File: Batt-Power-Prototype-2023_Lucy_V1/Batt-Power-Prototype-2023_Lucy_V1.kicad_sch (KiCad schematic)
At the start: 49 parts, among them J3 DE9_Receptacle_MountingHoles

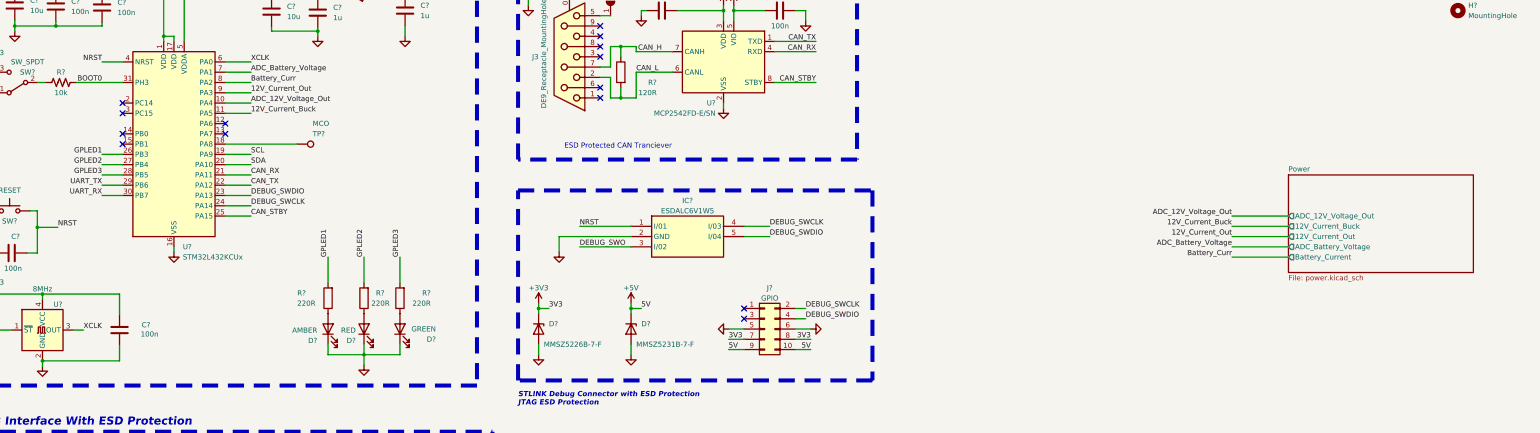
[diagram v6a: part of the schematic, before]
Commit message: everything but the battery input done
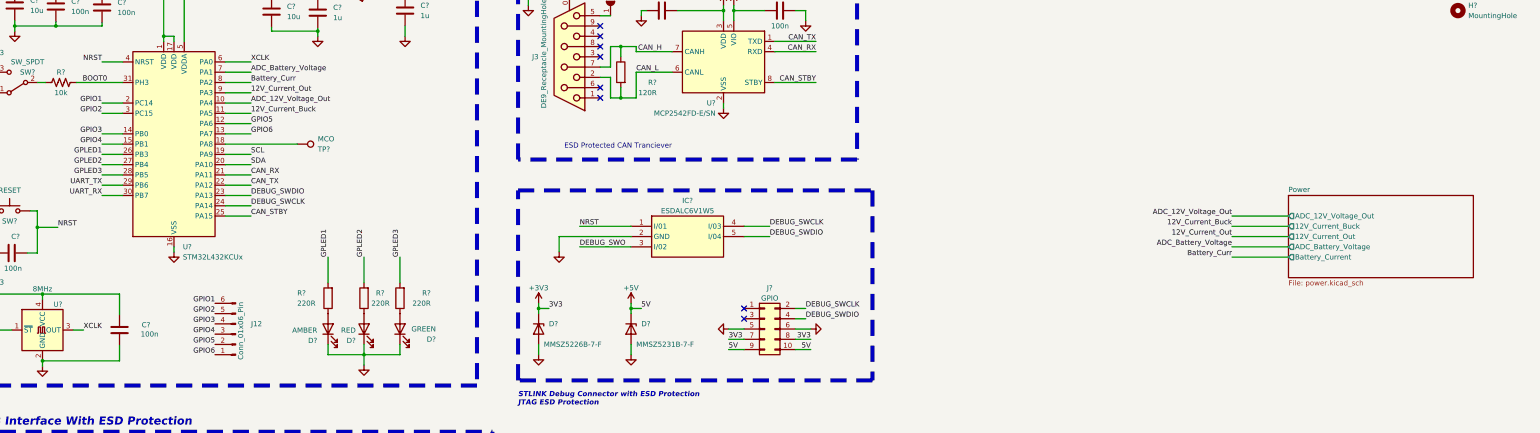
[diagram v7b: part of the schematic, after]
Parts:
- added J12: Conn_01x06_Pin, Connector_TE-Connectivity:TE_826576-6_1x06_P3.96mm_Vertical, symbol Connector:Conn_01x06_Pin
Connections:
- net GPIO5: now reaches U?.12 (PA6)
- net GPIO5: now also J12.2 (Pin_2)
- net GPIO6: now reaches U?.13 (PA7)
- net GPIO6: now also J12.1 (Pin_1)
- net GPIO3: now reaches U?.14 (PB0)
- net GPIO3: now also J12.4 (Pin_4)
- net GPIO4: now reaches U?.15 (PB1)
- net GPIO4: now also J12.3 (Pin_3)
- net GPIO1: now reaches U?.2 (PC14)
- net GPIO1: now also J12.6 (Pin_6)
- net GPIO2: now reaches U?.3 (PC15)
- net GPIO2: now also J12.5 (Pin_5)
- no-connect marks 19 -> 13
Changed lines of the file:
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@@
   (no_connect (at 176.53 45.72))
   (no_connect (at 54.61 160.02))
-  (no_connect (at 58.42 57.15))
   (no_connect (at 212.09 110.49))
-  (no_connect (at 58.42 59.69))
   (no_connect (at 176.53 53.34))
   (no_connect (at 31.75 167.64))
-  (no_connect (at 83.82 64.77))
   (no_connect (at 176.53 43.18))
   (no_connect (at 212.09 107.95))
   (no_connect (at 176.53 40.64))
-  (no_connect (at 58.42 67.31))
-  (no_connect (at 58.42 64.77))
   (no_connect (at 176.53 38.1))
   (no_connect (at 54.61 165.1))
-  (no_connect (at 83.82 62.23))
   (no_connect (at 31.75 162.56))
   (no_connect (at 176.53 55.88))
@@
     (stroke (width 0) (type default))
   )
+  (wire (pts (xy 83.82 62.23) (xy 90.17 62.23))
+    (stroke (width 0) (type default))
+  )
   (wire (pts (xy 57.15 147.32) (xy 55.88 147.32))
     (stroke (width 0) (type default))
@@
     (stroke (width 0) (type default))
   )
+  (wire (pts (xy 53.34 64.77) (xy 58.42 64.77))
+    (stroke (width 0) (type default))
+  )
   (wire (pts (xy 49.53 190.5) (xy 49.53 191.77))
     (stroke (width 0) (type default))
@@
     (stroke (width 0) (type default))
   )
+  (wire (pts (xy 53.34 59.69) (xy 58.42 59.69))
+    (stroke (width 0) (type default))
+  )
   (wire (pts (xy 186.69 34.29) (xy 186.69 35.56))
     (stroke (width 0) (type default))
@@
     (stroke (width 0) (type default))
   )
+  (wire (pts (xy 83.82 64.77) (xy 90.17 64.77))
+    (stroke (width 0) (type default))
+  )
   (wire (pts (xy 88.9 166.37) (xy 88.9 167.64))
     (stroke (width 0) (type default))
@@
     (stroke (width 0) (type default))
   )
+  (wire (pts (xy 53.34 67.31) (xy 58.42 67.31))
+    (stroke (width 0) (type default))
+  )
   (wire (pts (xy 31.75 38.1) (xy 31.75 39.37))
     (stroke (width 0) (type default))
@@
     (stroke (width 0) (type default))
   )
+  (wire (pts (xy 53.34 57.15) (xy 58.42 57.15))
+    (stroke (width 0) (type default))
+  )
   (wire (pts (xy 30.48 180.34) (xy 30.48 182.88))
     (stroke (width 0) (type default))
@@
     (effects (font (size 1.27 1.27)) (justify left bottom))
   )
+  (label "GPIO3" (at 81.28 111.76 180) (fields_autoplaced)
+    (effects (font (size 1.27 1.27)) (justify right bottom))
+  )
   (label "5V" (at 186.69 107.95 0) (fields_autoplaced)
     (effects (font (size 1.27 1.27)) (justify left bottom))
@@
     (effects (font (size 1.27 1.27)) (justify left bottom))
   )
+  (label "GPIO5" (at 81.28 116.84 180) (fields_autoplaced)
+    (effects (font (size 1.27 1.27)) (justify right bottom))
+  )
   (label "5V" (at 208.28 118.11 0) (fields_autoplaced)
     (effects (font (size 1.27 1.27)) (justify left bottom))
   )
+  (label "GPIO1" (at 81.28 106.68 180) (fields_autoplaced)
+    (effects (font (size 1.27 1.27)) (justify right bottom))
+  )
   (label "GPLED1" (at 53.34 69.85 180) (fields_autoplaced)
     (effects (font (size 1.27 1.27)) (justify right bottom))
@@
     (effects (font (size 1.27 1.27)) (justify right bottom))
   )
+  (label "GPIO2" (at 81.28 109.22 180) (fields_autoplaced)
+    (effects (font (size 1.27 1.27)) (justify right bottom))
+  )
+  (label "GPIO5" (at 90.17 62.23 0) (fields_autoplaced)
+    (effects (font (size 1.27 1.27)) (justify left bottom))
+  )
+  (label "GPIO6" (at 90.17 64.77 0) (fields_autoplaced)
+    (effects (font (size 1.27 1.27)) (justify left bottom))
+  )
   (label "DEBUG_SWDIO" (at 90.17 80.01 0) (fields_autoplaced)
     (effects (font (size 1.27 1.27)) (justify left bottom))
   )
+  (label "GPIO3" (at 53.34 64.77 180) (fields_autoplaced)
+    (effects (font (size 1.27 1.27)) (justify right bottom))
+  )
   (label "UART_RX" (at 53.34 80.01 180) (fields_autoplaced)
     (effects (font (size 1.27 1.27)) (justify right bottom))
@@
     (effects (font (size 1.27 1.27)) (justify right bottom))
   )
+  (label "GPIO1" (at 53.34 57.15 180) (fields_autoplaced)
+    (effects (font (size 1.27 1.27)) (justify right bottom))
+  )
+  (label "GPIO6" (at 81.28 119.38 180) (fields_autoplaced)
+    (effects (font (size 1.27 1.27)) (justify right bottom))
+  )
   (label "GPLED2" (at 118.11 95.25 90) (fields_autoplaced)
     (effects (font (size 1.27 1.27)) (justify left bottom))
@@
     (effects (font (size 1.27 1.27)) (justify left bottom))
   )
+  (label "GPIO2" (at 53.34 59.69 180) (fields_autoplaced)
+    (effects (font (size 1.27 1.27)) (justify right bottom))
+  )
   (label "CAN_STBY" (at 90.17 85.09 0) (fields_autoplaced)
     (effects (font (size 1.27 1.27)) (justify left bottom))
@@
     (effects (font (size 1.27 1.27)) (justify right bottom))
   )
-  (label "BOOT0" (at 53.34 52.07 180) (fields_autoplaced)
+  (label "BOOT0" (at 54.61 52.07 180) (fields_autoplaced)
     (effects (font (size 1.27 1.27)) (justify right bottom))
   )
@@
     (effects (font (size 1.27 1.27)) (justify right bottom))
   )
+  (label "GPIO4" (at 53.34 67.31 180) (fields_autoplaced)
+    (effects (font (size 1.27 1.27)) (justify right bottom))
+  )
+  (label "GPIO4" (at 81.28 114.3 180) (fields_autoplaced)
+    (effects (font (size 1.27 1.27)) (justify right bottom))
+  )
   (label "NRST" (at 53.34 46.99 180) (fields_autoplaced)
     (effects (font (size 1.27 1.27)) (justify right bottom))
@@
   (symbol (lib_id "Connector:TestPoint") (at 101.6 67.31 270) (unit 1)
     (in_bom yes) (on_board yes) (dnp no)
-    (property "Reference" "TP?" (at 105.41 64.77 90)
+    (property "Reference" "TP?" (at 106.68 68.58 90)
       (effects (font (size 1.27 1.27)) (justify left))
     )
-    (property "Value" "MCO" (at 105.41 62.23 90)
+    (property "Value" "MCO" (at 106.68 66.04 90)
       (effects (font (size 1.27 1.27)) (justify left))
     )
@@
     )
   )
+  (symbol (lib_id "Connector:Conn_01x06_Pin") (at 86.36 114.3 180) (unit 1)
+    (in_bom yes) (on_board yes) (dnp no)
+    (property "Reference" "J12" (at 90.17 111.76 0)
+      (effects (font (size 1.27 1.27)) (justify right))
+    )
+    (property "Value" "Conn_01x06_Pin" (at 87.63 120.65 90)
+      (effects (font (size 1.27 1.27)) (justify right))
+    )
+    (property "Footprint" "Connector_TE-Connectivity:TE_826576-6_1x06_P3.96mm_Vertical" (at 86.36 114.3 0)
+      (effects (font (size 1.27 1.27)) hide)
+    )
+    (property "Datasheet" "~" (at 86.36 114.3 0)
+      (effects (font (size 1.27 1.27)) hide)
+    )
+    (pin "1")
+    (pin "2")
+    (pin "3")
+    (pin "4")
+    (pin "5")
+    (pin "6")
+    (instances
+      (project "Batt-Power-Prototype-2023_Lucy_V1"
+        (path "/c58627b7-5b67-4b57-b29b-cc34a75a9096"
+          (reference "J12") (unit 1)
+        )
+      )
+    )
+  )
   (symbol (lib_id "MCU_ST_STM32L4:STM32L432KCUx") (at 71.12 67.31 0) (unit 1)
     (in_bom yes) (on_board yes) (dnp no) (fields_autoplaced)
@@
     )
   )
-  (sheet (at 346.71 74.93) (size 45.72 24.13) (fields_autoplaced)
+  (sheet (at 346.71 80.01) (size 45.72 20.32) (fields_autoplaced)
     (stroke (width 0.1524) (type solid))
     (fill (color 0 0 0 0.0000))
-    (property "Sheetname" "Power" (at 346.71 74.2184 0)
+    (property "Sheetname" "Power" (at 346.71 79.2984 0)
       (effects (font (size 1.27 1.27)) (justify left bottom))
     )
-    (property "Sheetfile" "power.kicad_sch" (at 346.71 99.6446 0)
+    (property "Sheetfile" "power.kicad_sch" (at 346.71 100.9146 0)
       (effects (font (size 1.27 1.27)) (justify left top))
     )

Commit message: everything done?!
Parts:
- C? (x2): JLCPCB Part#(optional) C1671 -> (none)
- C? (x9): JLCPCB Part#(optional) C1525 -> (none)
- C?: JLCPCB Part#(optional) C1779 -> (none)
- C? (x2): JLCPCB Part#(optional) C96446 -> (none)
- C? (x2): JLCPCB Part#(optional) C28323 -> (none)
- D? (x2): JLCPCB Part#(optional) C2296 -> (none)
- D?: JLCPCB Part#(optional) C2297 -> (none)
- D?: JLCPCB Part#(optional) C84256 -> (none)
- D?: DK # 497-5235-1-ND -> (none); Digikey # (none) -> 497-5235-1-ND
- FB?: DK # 1934-1474-1-ND -> (none); Digikey # (none) -> 1934-1474-1-ND
- IC?: DK # 497-7231-1-ND -> (none); Digikey # (none) -> 497-7231-1-ND
- J?: DK # 609-4618-1-ND -> (none); Digikey # (none) -> 609-4618-1-ND
- R? (x4): JLCPCB Part#(optional) C17557 -> (none)
- R? (x2): JLCPCB Part#(optional) C25190 -> (none)
- R?: JLCPCB Part#(optional) C17414 -> (none)
- SW?: DK # 2223-SLW-66527511-SMT-TRCT-ND -> (none); Digikey # (none) -> 2223-SLW-66527511-SMT-TRCT-ND
- U?: DK # 535-ASE-8.000MHZ-L-C-TCT-ND -> (none); Digikey # (none) -> 535-ASE-8.000MHZ-L-C-TCT-ND
- U?: DK # 768-1178-1-ND -> (none); Digikey # (none) -> 768-1178-1-ND; JLCPCB Part#(optional) C132158 -> (none)
- U?: DK # MCP2542FD-E/SN-ND -> (none); Digikey # (none) -> MCP2542FD-E/SN-ND
- U?: JLCPCB Part#(optional) C1337280 -> (none)
